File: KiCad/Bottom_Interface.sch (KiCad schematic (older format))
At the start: 1 part, among them U2 iCE40-HX8K-CT256

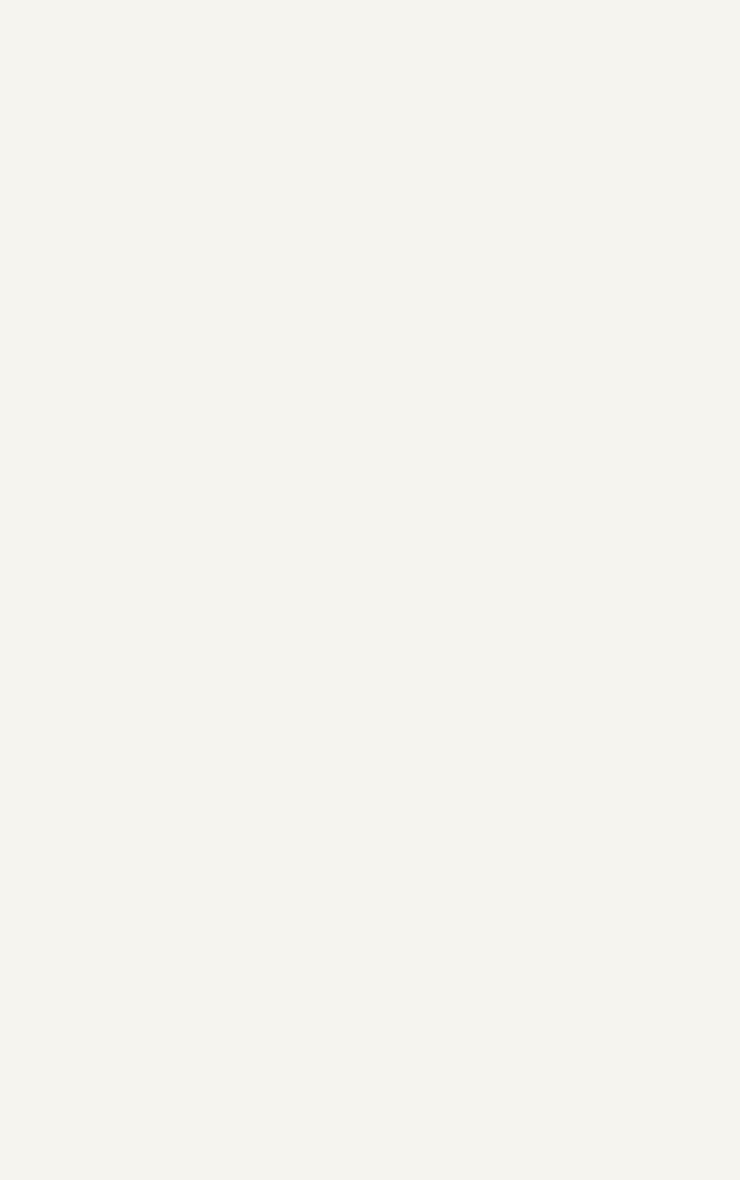
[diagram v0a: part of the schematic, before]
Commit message: working on bottom FPGA
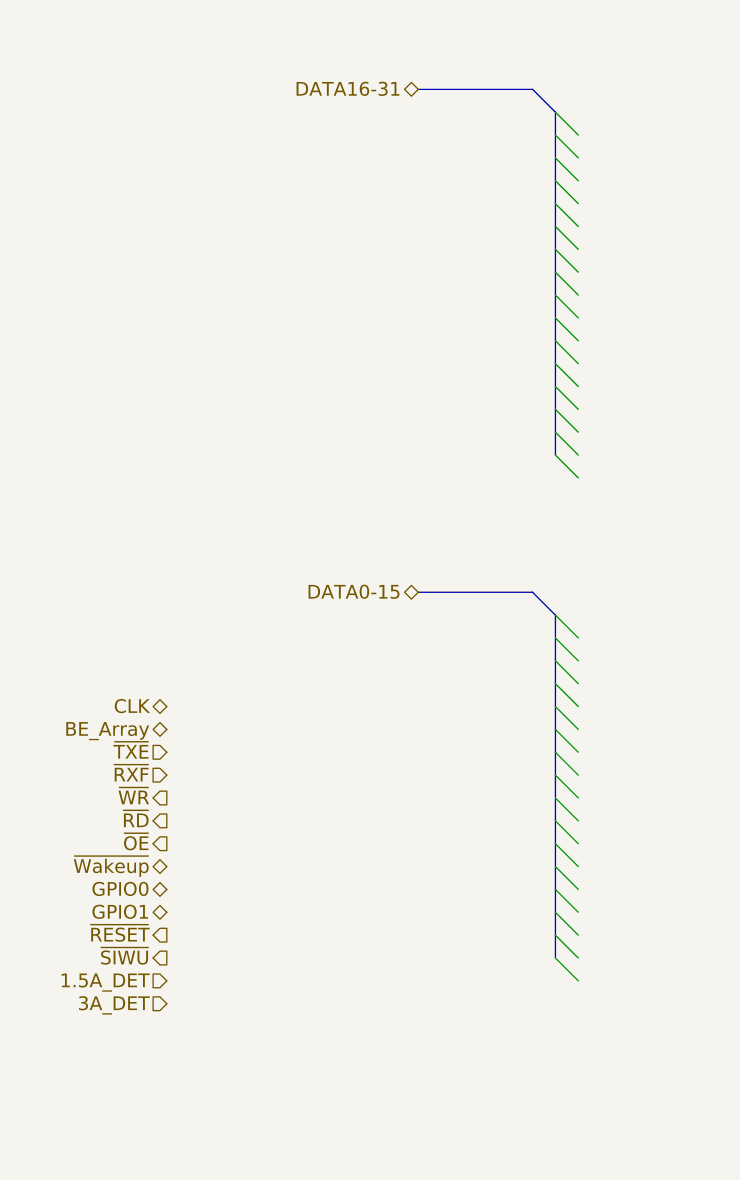
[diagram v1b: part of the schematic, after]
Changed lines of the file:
@@
 	1    0    0    -1
 $EndComp
+Text HLabel 6500 1100 0    60   BiDi ~ 0
+DATA16-31
+Text HLabel 6500 3300 0    60   BiDi ~ 0
+DATA0-15
+Text HLabel 5400 3800 0    60   BiDi ~ 0
+CLK
+Text HLabel 5400 3900 0    60   BiDi ~ 0
+BE_Array
+Text HLabel 5400 4000 0    60   Input ~ 0
+~TXE
+Text HLabel 5400 4100 0    60   Input ~ 0
+~RXF
+Text HLabel 5400 4200 0    60   Output ~ 0
+~WR
+Text HLabel 5400 4300 0    60   Output ~ 0
+~RD
+Text HLabel 5400 4400 0    60   Output ~ 0
+~OE
+Text HLabel 5400 4500 0    60   BiDi ~ 0
+~Wakeup
+Text HLabel 5400 4600 0    60   BiDi ~ 0
+GPIO0
+Text HLabel 5400 4700 0    60   BiDi ~ 0
+GPIO1
+Text HLabel 5400 4800 0    60   Output ~ 0
+~RESET
+Text HLabel 5400 4900 0    60   Output ~ 0
+~SIWU
+Text HLabel 5400 5000 0    60   Input ~ 0
+1.5A_DET
+Text HLabel 5400 5100 0    60   Input ~ 0
+3A_DET
+Wire Bus Line
+	6500 1100 7000 1100
+Wire Bus Line
+	7000 1100 7100 1200
+Wire Bus Line
+	7100 1200 7100 1300
+Wire Bus Line
+	7100 1300 7100 1400
+Wire Bus Line
+	7100 1400 7100 1500
+Wire Bus Line
+	7100 1500 7100 1600
+Wire Bus Line
+	7100 1600 7100 1700
+Wire Bus Line
+	7100 1700 7100 1800
+Wire Bus Line
+	7100 1800 7100 1900
+Wire Bus Line
+	7100 1900 7100 2000
+Wire Bus Line
+	7100 2000 7100 2100
+Wire Bus Line
+	7100 2100 7100 2200
+Wire Bus Line
+	7100 2200 7100 2300
+Wire Bus Line
+	7100 2300 7100 2400
+Wire Bus Line
+	7100 2400 7100 2500
+Wire Bus Line
+	7100 2500 7100 2600
+Wire Bus Line
+	7100 2600 7100 2700
+Entry Wire Line
+	7100 2700 7200 2800
+Entry Wire Line
+	7100 2600 7200 2700
+Entry Wire Line
+	7100 2500 7200 2600
+Entry Wire Line
+	7100 2400 7200 2500
+Entry Wire Line
+	7100 2300 7200 2400
+Entry Wire Line
+	7100 2200 7200 2300
+Entry Wire Line
+	7100 2100 7200 2200
+Entry Wire Line
+	7100 2000 7200 2100
+Entry Wire Line
+	7100 1900 7200 2000
+Entry Wire Line
+	7100 1800 7200 1900
+Entry Wire Line
+	7100 1700 7200 1800
+Entry Wire Line
+	7100 1600 7200 1700
+Entry Wire Line
+	7100 1500 7200 1600
+Entry Wire Line
+	7100 1400 7200 1500
+Entry Wire Line
+	7100 1300 7200 1400
+Entry Wire Line
+	7100 1200 7200 1300
+Wire Bus Line
+	6500 3300 7000 3300
+Wire Bus Line
+	7000 3300 7100 3400
+Wire Bus Line
+	7100 3400 7100 3500
+Wire Bus Line
+	7100 3500 7100 3600
+Wire Bus Line
+	7100 3600 7100 3700
+Wire Bus Line
+	7100 3700 7100 3800
+Wire Bus Line
+	7100 3800 7100 3900
+Wire Bus Line
+	7100 3900 7100 4000
+Wire Bus Line
+	7100 4000 7100 4100
+Wire Bus Line
+	7100 4100 7100 4200
+Wire Bus Line
+	7100 4200 7100 4300
+Wire Bus Line
+	7100 4300 7100 4400
+Wire Bus Line
+	7100 4400 7100 4500
+Wire Bus Line
+	7100 4500 7100 4600
+Wire Bus Line
+	7100 4600 7100 4700
+Wire Bus Line
+	7100 4700 7100 4800
+Wire Bus Line
+	7100 4800 7100 4900
+Entry Wire Line
+	7100 4900 7200 5000
+Entry Wire Line
+	7100 4800 7200 4900
+Entry Wire Line
+	7100 4700 7200 4800
+Entry Wire Line
+	7100 4600 7200 4700
+Entry Wire Line
+	7100 4500 7200 4600
+Entry Wire Line
+	7100 4400 7200 4500
+Entry Wire Line
+	7100 4300 7200 4400
+Entry Wire Line
+	7100 4200 7200 4300
+Entry Wire Line
+	7100 4100 7200 4200
+Entry Wire Line
+	7100 4000 7200 4100
+Entry Wire Line
+	7100 3900 7200 4000
+Entry Wire Line
+	7100 3800 7200 3900
+Entry Wire Line
+	7100 3700 7200 3800
+Entry Wire Line
+	7100 3600 7200 3700
+Entry Wire Line
+	7100 3500 7200 3600
+Entry Wire Line
+	7100 3400 7200 3500
 $EndSCHEMATC

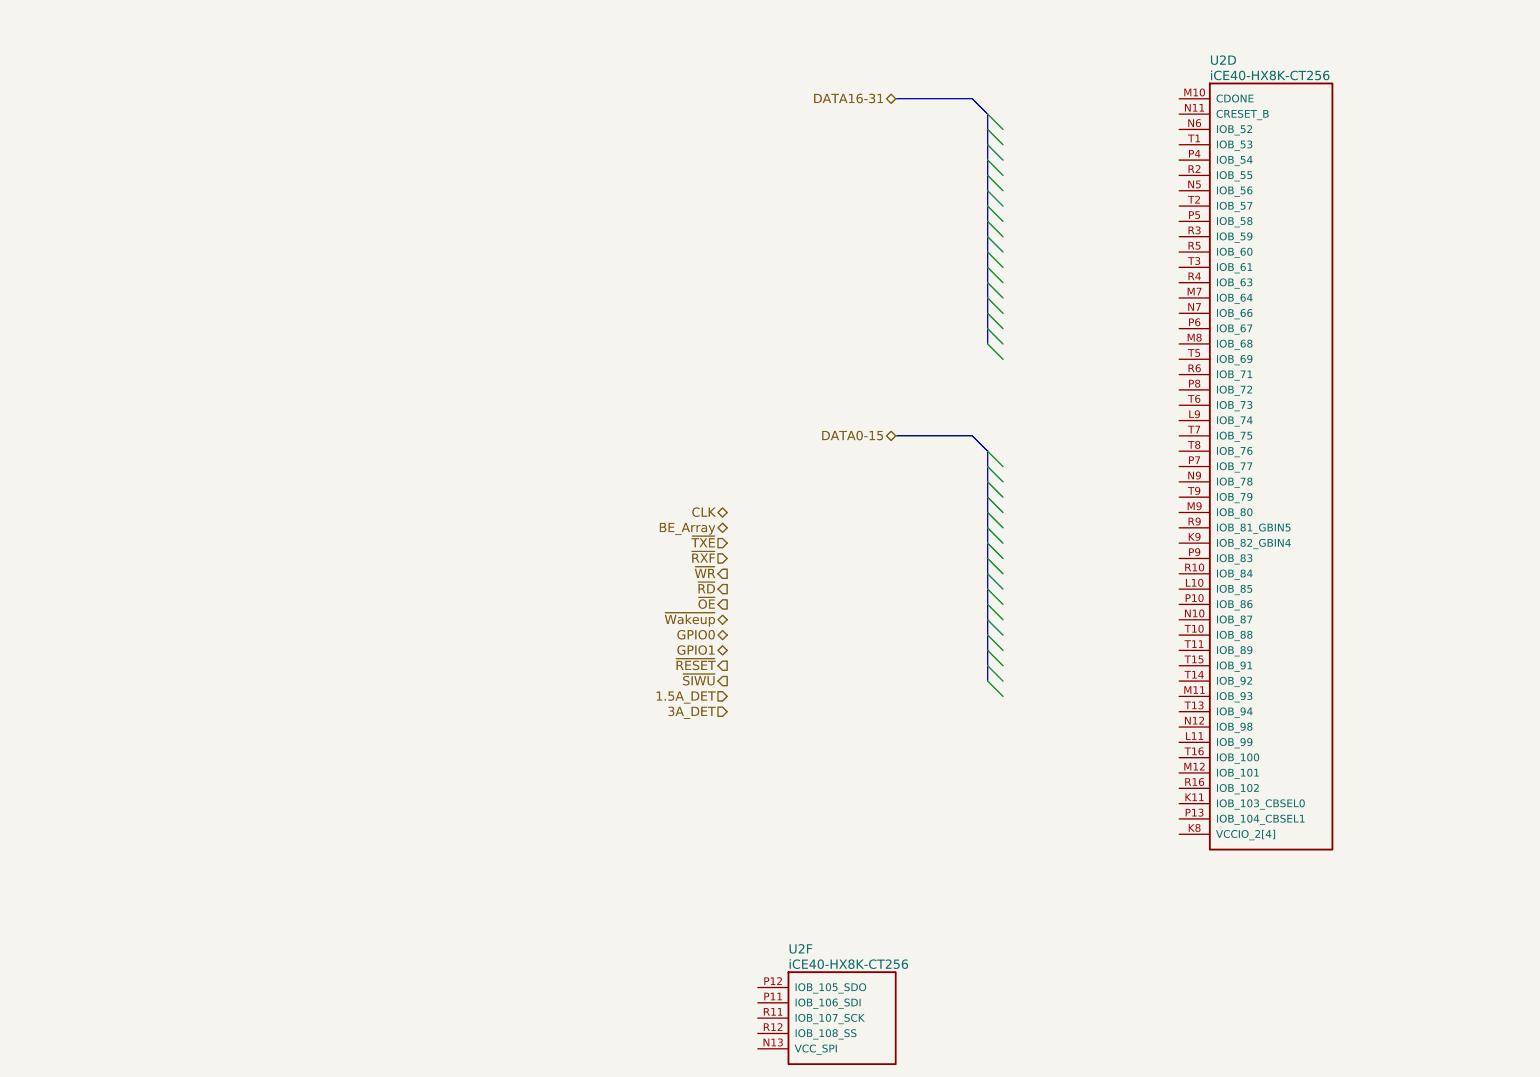
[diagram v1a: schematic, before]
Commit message: fix bus route
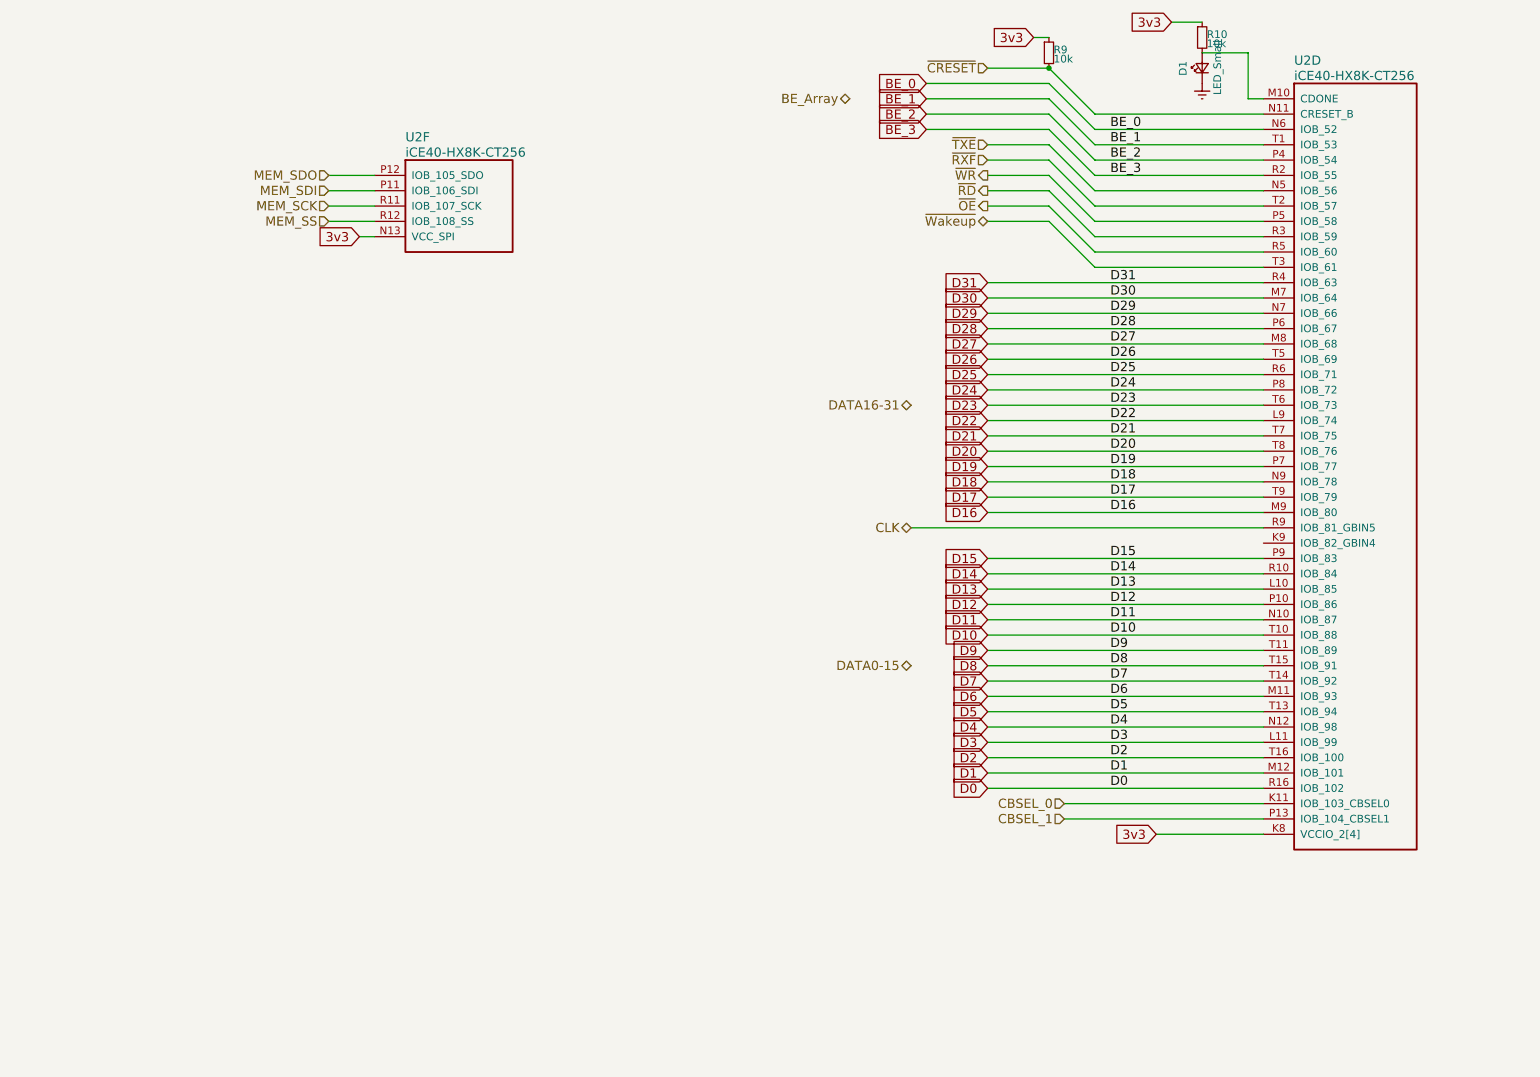
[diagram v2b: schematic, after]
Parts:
- added D1: LED_Small, LEDs:LED_0603, symbol LED_Small
- added R10, R9: 10k, Resistors_SMD:R_0603, symbol R_Small
- U2: footprint (none) -> Homebrew:caBGA_256_.8p_14x14mm
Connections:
- net CLK: now also U2.R9 (IOB_81_GBIN5)
- net ~OE: now also U2.R5 (IOB_60)
- net ~RD: now also U2.R3 (IOB_59)
- net ~RXF: now also U2.T2 (IOB_57)
- net ~TXE: now also U2.N5 (IOB_56)
- net ~WR: now also U2.P5 (IOB_58)
- net ~Wakeup: now also U2.T3 (IOB_61)
- net CBSEL_0: now reaches U2.K11 (IOB_103_CBSEL0)
- net 3v3: now reaches U2.K8 (VCCIO_2[4]), U2.P3 (VCCIO_2[4]), U2.R13 (VCCIO_2[4]), U2.R8 (VCCIO_2[4])
- net 3v3: now also U2.N13 (VCC_SPI), R10.1, R9.1
- net D13: now reaches U2.L10 (IOB_85)
- net D3: now reaches U2.L11 (IOB_99)
- net D22: now reaches U2.L9 (IOB_74)
- net at U2.M10 (CDONE): now also D1.2 (A), R10.2
- net D6: now reaches U2.M11 (IOB_93)
- net D1: now reaches U2.M12 (IOB_101)
- net D30: now reaches U2.M7 (IOB_64)
- net D27: now reaches U2.M8 (IOB_68)
- net D16: now reaches U2.M9 (IOB_80)
- net D11: now reaches U2.N10 (IOB_87)
- net ~CRESET: now reaches U2.N11 (CRESET_B)
- net ~CRESET: now also R9.2
- net D4: now reaches U2.N12 (IOB_98)
- net BE_0: now reaches U2.N6 (IOB_52)
- net D29: now reaches U2.N7 (IOB_66)
- net D18: now reaches U2.N9 (IOB_78)
- net D12: now reaches U2.P10 (IOB_86)
- net CBSEL_1: now reaches U2.P13 (IOB_104_CBSEL1)
- net BE_2: now reaches U2.P4 (IOB_54)
- net D28: now reaches U2.P6 (IOB_67)
- net D19: now reaches U2.P7 (IOB_77)
- net D24: now reaches U2.P8 (IOB_72)
- net D15: now reaches U2.P9 (IOB_83)
- net D14: now reaches U2.R10 (IOB_84)
- net D0: now reaches U2.R16 (IOB_102)
- net BE_3: now reaches U2.R2 (IOB_55)
- net D31: now reaches U2.R4 (IOB_63)
- net D25: now reaches U2.R6 (IOB_71)
- net BE_1: now reaches U2.T1 (IOB_53)
- net D10: now reaches U2.T10 (IOB_88)
- net D9: now reaches U2.T11 (IOB_89)
- net D5: now reaches U2.T13 (IOB_94)
- net D7: now reaches U2.T14 (IOB_92)
- net D8: now reaches U2.T15 (IOB_91)
- net D2: now reaches U2.T16 (IOB_100)
- net D26: now reaches U2.T5 (IOB_69)
- net D23: now reaches U2.T6 (IOB_73)
- net D21: now reaches U2.T7 (IOB_75)
- net D20: now reaches U2.T8 (IOB_76)
- net D17: now reaches U2.T9 (IOB_79)
- net MEM_SDI: now reaches U2.P11 (IOB_106_SDI)
- net MEM_SDO: now reaches U2.P12 (IOB_105_SDO)
- net MEM_SCK: now reaches U2.R11 (IOB_107_SCK)
- net MEM_SS: now reaches U2.R12 (IOB_108_SS)
- new net Earth: D1.1 (K)
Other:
- moved on the sheet: U2D, U2F

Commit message: top routed?
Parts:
- added C9: .1uF, Capacitors_SMD:C_0402, symbol C_Small
- added M1: CLOCK_EN, Crystals:Crystal_SMD_EuroQuartz_MT-4pin_3.2x2.5mm, symbol CLOCK_EN
- added unit 3 of U2
- R10, R9: footprint Resistors_SMD:R_0603 -> Resistors_SMD:R_0402
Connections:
- net labels added: 50MHz
- wire segments 79 -> 59
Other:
- moved on the sheet: D1, R10, R9, U2D, U2F

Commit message: 10_20_2017 update
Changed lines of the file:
@@
 LIBS:Homebrew
 LIBS:Super_Blaster_v0.1-cache
-EELAYER 25 0
+EELAYER 26 0
 EELAYER END
 $Descr A4 11693 8268
@@
 	1    0    0    -1
 $EndComp
-Text HLabel 5100 1400 0    60   BiDi ~ 0
+Text HLabel 5200 2100 0    60   BiDi ~ 0
 DATA16-31
-Text HLabel 8300 2800 0    60   BiDi ~ 0
+Text HLabel 8500 900  0    60   BiDi ~ 0
 DATA0-15
 Text HLabel 5800 4000 0    60   BiDi ~ 0
@@
 $EndComp
 $Comp
-L Earth #PWR026
+L Earth #PWR27
 U 1 1 5910C679
 P 6200 1100
-F 0 "#PWR026" H 6200 850 50  0001 C CNN
+F 0 "#PWR27" H 6200 850 50  0001 C CNN
 F 1 "Earth" H 6200 950 50  0001 C CNN
 F 2 "" H 6200 1100 50  0001 C CNN
@@
 $EndComp
 $Comp
-L Earth #PWR027
+L Earth #PWR26
 U 1 1 591371AB
 P 1500 7000
-F 0 "#PWR027" H 1500 6750 50  0001 C CNN
+F 0 "#PWR26" H 1500 6750 50  0001 C CNN
 F 1 "Earth" H 1500 6850 50  0001 C CNN
 F 2 "" H 1500 7000 50  0001 C CNN
@@
 	2000 4500 2900 4500
 Wire Notes Line
-	5400 1500 5400 4700
-Wire Notes Line
-	5400 1500 5300 1400
-Wire Notes Line
-	5300 1400 5100 1400
-Wire Notes Line
-	8600 2900 8600 6000
-Wire Notes Line
-	8500 2800 8600 2900
-Wire Notes Line
-	8300 2800 8500 2800
+	5500 2200 5500 5700
+Wire Notes Line
+	5500 2200 5400 2100
+Wire Notes Line
+	5400 2100 5200 2100
+Wire Notes Line
+	8800 1000 8800 4700
+Wire Notes Line
+	8700 900  8800 1000
+Wire Notes Line
+	8500 900  8700 900
 Wire Notes Line
 	1400 4100 1600 4100
